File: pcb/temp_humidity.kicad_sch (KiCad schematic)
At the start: 2 parts, among them U6 AHT20-F

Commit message: sch: move usb to separate sheet
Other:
- note added: "AHT20"
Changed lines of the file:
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@@
 	(generator_version "10.0")
 	(paper "A4")
+	(rectangle
+		(start 21.59 15.24)
+		(end 66.04 55.88)
+		(stroke
+			(width 0)
+			(type default)
+		)
+		(fill
+			(type none)
+		)
+	)
+	(text "AHT20"
+		(exclude_from_sim no)
+		(at 42.672 18.288 0)
+		(effects
+			(font
+				(size 1.27 1.27)
+			)
+		)
+	)
 	(junction
 		(at 40.64 27.94)

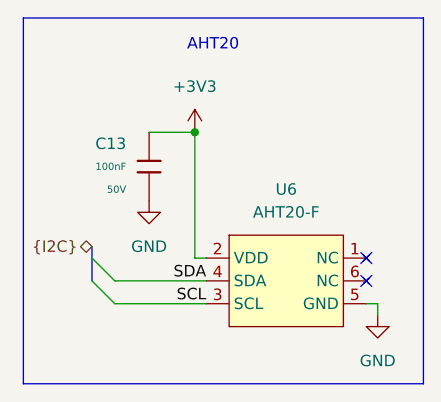
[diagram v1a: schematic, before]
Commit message: sch: replace mcu and clean up schematic
Fixes #27
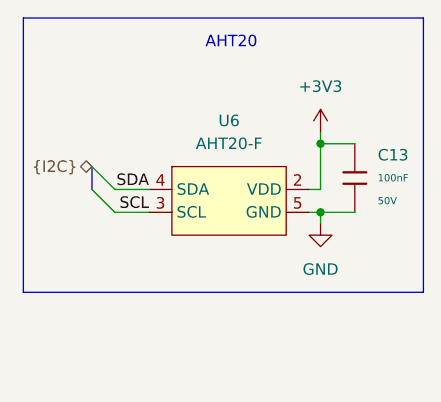
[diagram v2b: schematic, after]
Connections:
- no-connect marks 2 -> 0
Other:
- moved on the sheet: C13
